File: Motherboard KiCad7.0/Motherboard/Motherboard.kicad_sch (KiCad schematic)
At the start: 59 parts, among them J1 USB_B_Micro, J2 SWD_01x04_Pin, Q7 AO4447A, SW1 SW_STM_RESET, SW2 SW_STM_BOOT_MODE, U1 STM32F103CBT6, U2 AMS1117-3.3, U3 LM66100DCKR, U4 LM66100DCKR, U5 LM66100DCKR, U6 LMR51430XDDCR, Y1 X322516MMB4SI

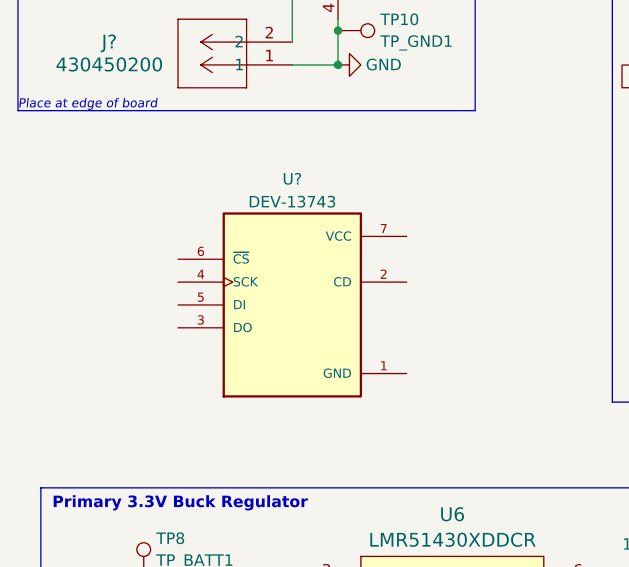
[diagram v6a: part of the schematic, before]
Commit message: Added I2C connector to schematic
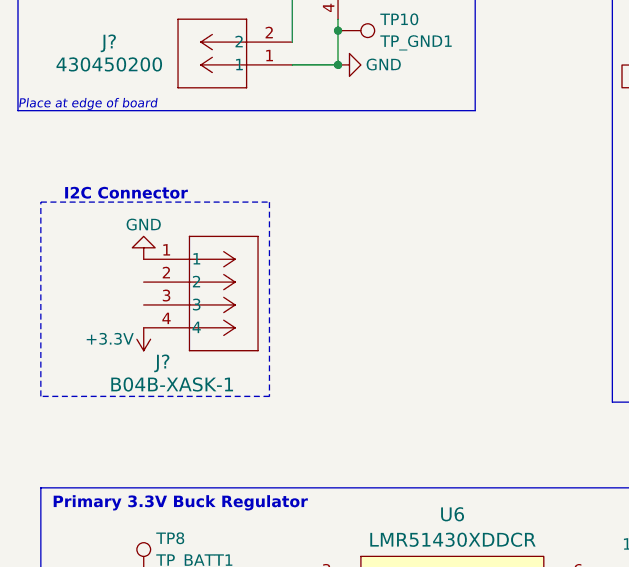
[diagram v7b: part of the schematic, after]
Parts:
- removed U?: DEV-13743, DEV-13743:MODULE_DEV-13743, symbol DEV-13743:DEV-13743
- added J?: B04B-XASK-1, B04B_XASK1:CONN_B04B-XASK-1_JST, symbol B04B_XASK_1:B04B-XASK-1
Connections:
- net +3.3V: now also J?.4
- net GND: now also J?.1
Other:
- note added: "I2C Connector"
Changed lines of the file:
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@@
+    (fill (type none))
+  )
+  (rectangle (start 17.78 52.07) (end 43.18 73.66)
+    (stroke (width 0) (type dash))
     (fill (type none))
   )
@@
   )
   (text "STM32 Decoupling Capacitors for VBAT and VDD" (at 140.97 17.145 0)
+    (effects (font (size 1.27 1.27) (thickness 0.254) bold) (justify left bottom))
+  )
+  (text "I2C Connector" (at 20.32 52.07 0)
     (effects (font (size 1.27 1.27) (thickness 0.254) bold) (justify left bottom))
   )
@@
     )
   )
+  (symbol (lib_id "B04B_XASK_1:B04B-XASK-1") (at 29.21 58.42 0) (unit 1)
+    (in_bom yes) (on_board yes) (dnp no)
+    (property "Reference" "J?" (at 30.48 69.85 0)
+      (effects (font (size 1.524 1.524)) (justify left))
+    )
+    (property "Value" "B04B-XASK-1" (at 25.4 72.39 0)
+      (effects (font (size 1.524 1.524)) (justify left))
+    )
+    (property "Footprint" "B04B_XASK1:CONN_B04B-XASK-1_JST" (at 26.67 52.07 0)
+      (effects (font (size 1.27 1.27) italic) hide)
+    )
+    (property "Datasheet" "B04B-XASK-1" (at 26.67 53.34 0)
+      (effects (font (size 1.27 1.27) italic) hide)
+    )
+    (property "LCSC" "C264994" (at 29.21 58.42 0)
+      (effects (font (size 1.27 1.27)) hide)
+    )
+    (property "Digikey" "455-2150-ND" (at 29.21 58.42 0)
+      (effects (font (size 1.27 1.27)) hide)
+    )
+    (pin "3")
+    (pin "1")
+    (pin "4")
+    (pin "2")
+    (instances
+      (project "Motherboard"
+        (path "/6c6aab7b-9fc7-4161-8073-41667e18c629"
+          (reference "J?") (unit 1)
+        )
+      )
+    )
+  )
   (symbol (lib_id "Switch:SW_Push") (at 54.61 176.53 0) (unit 1)
     (in_bom yes) (on_board yes) (dnp no) (fields_autoplaced)
@@
     )
   )
+  (symbol (lib_id "power:+3.3V") (at 29.21 66.04 0) (mirror x) (unit 1)
+    (in_bom yes) (on_board yes) (dnp no)
+    (property "Reference" "#PWR045" (at 29.21 62.23 0)
+      (effects (font (size 1.27 1.27)) hide)
+    )
+    (property "Value" "+3.3V" (at 25.4 67.31 0)
+      (effects (font (size 1.27 1.27)))
+    )
+    (property "Footprint" "" (at 29.21 66.04 0)
+      (effects (font (size 1.27 1.27)) hide)
+    )
+    (property "Datasheet" "" (at 29.21 66.04 0)
+      (effects (font (size 1.27 1.27)) hide)
+    )
+    (pin "1")
+    (instances
+      (project "Motherboard"
+        (path "/6c6aab7b-9fc7-4161-8073-41667e18c629"
+          (reference "#PWR045") (unit 1)
+        )
+      )
+    )
+  )
   (symbol (lib_id "Connector:TestPoint") (at 109.855 142.24 0) (unit 1)
     (in_bom yes) (on_board yes) (dnp no)
@@
         (path "/6c6aab7b-9fc7-4161-8073-41667e18c629"
           (reference "#PWR04") (unit 1)
+        )
+      )
+    )
+  )
+  (symbol (lib_id "power:GND") (at 29.21 58.42 180) (unit 1)
+    (in_bom yes) (on_board yes) (dnp no)
+    (property "Reference" "#PWR044" (at 29.21 52.07 0)
+      (effects (font (size 1.27 1.27)) hide)
+    )
+    (property "Value" "GND" (at 29.21 54.61 0)
+      (effects (font (size 1.27 1.27)))
+    )
+    (property "Footprint" "" (at 29.21 58.42 0)
+      (effects (font (size 1.27 1.27)) hide)
+    )
+    (property "Datasheet" "" (at 29.21 58.42 0)
+      (effects (font (size 1.27 1.27)) hide)
+    )
+    (pin "1")
+    (instances
+      (project "Motherboard"
+        (path "/6c6aab7b-9fc7-4161-8073-41667e18c629"
+          (reference "#PWR044") (unit 1)
         )
       )
@@
         )
       )
-    )
-  )
-  (symbol (lib_id "DEV-13743:DEV-13743") (at 45.72 63.5 0) (unit 1)
-    (in_bom yes) (on_board yes) (dnp no) (fields_autoplaced)
-    (property "Reference" "U?" (at 45.72 49.53 0)
-      (effects (font (size 1.27 1.27)))
-    )
-    (property "Value" "DEV-13743" (at 45.72 52.07 0)
-      (effects (font (size 1.27 1.27)))
-    )
-    (property "Footprint" "DEV-13743:MODULE_DEV-13743" (at 45.72 63.5 0)
-      (effects (font (size 1.27 1.27)) (justify bottom) hide)
-    )
-    (property "Datasheet" "" (at 45.72 63.5 0)
-      (effects (font (size 1.27 1.27)) hide)
-    )
-    (property "PARTREV" "N/A" (at 45.72 63.5 0)
-      (effects (font (size 1.27 1.27)) (justify bottom) hide)
-    )
-    (property "MANUFACTURER" "Sparkfun Electronics" (at 45.72 63.5 0)
-      (effects (font (size 1.27 1.27)) (justify bottom) hide)
-    )
-    (property "MAXIMUM_PACKAGE_HEIGHT" "6.0 mm" (at 45.72 63.5 0)
-      (effects (font (size 1.27 1.27)) (justify bottom) hide)
-    )
-    (property "STANDARD" "Manufacturer Recommendations" (at 45.72 63.5 0)
-      (effects (font (size 1.27 1.27)) (justify bottom) hide)
-    )
-    (property "Digikey" "1568-1356-ND" (at 45.72 63.5 0)
-      (effects (font (size 1.27 1.27)) hide)
-    )
-    (pin "3")
-    (pin "4")
-    (pin "6")
-    (pin "1")
-    (pin "7")
-    (pin "2")
-    (pin "5")
-    (instances
-      (project "Motherboard"
-        (path "/6c6aab7b-9fc7-4161-8073-41667e18c629"
-          (reference "U?") (unit 1)
-        )
-      )

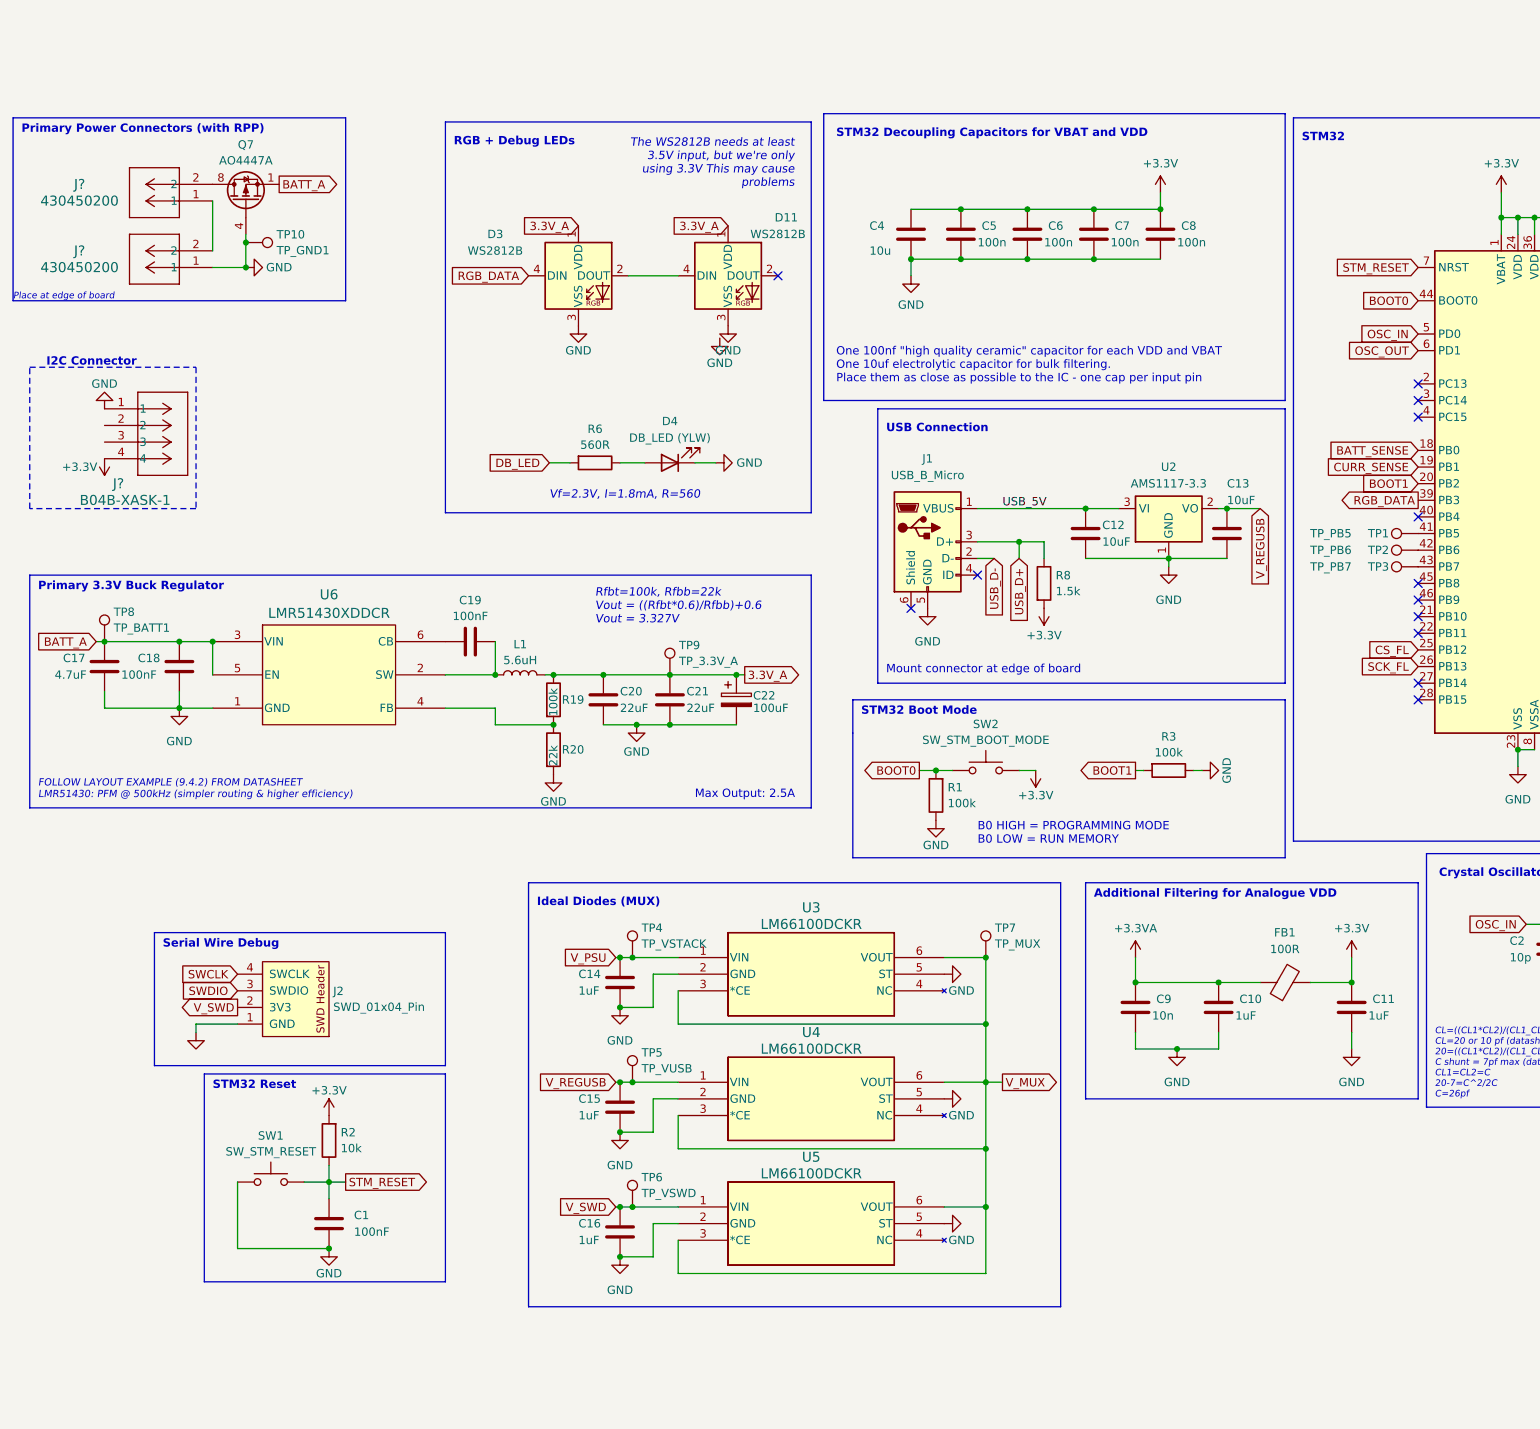
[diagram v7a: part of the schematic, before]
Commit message: Updated symbols and fixed circuit
Updated outdated symbols and replaced 3.3V buck converter circuit with a module.
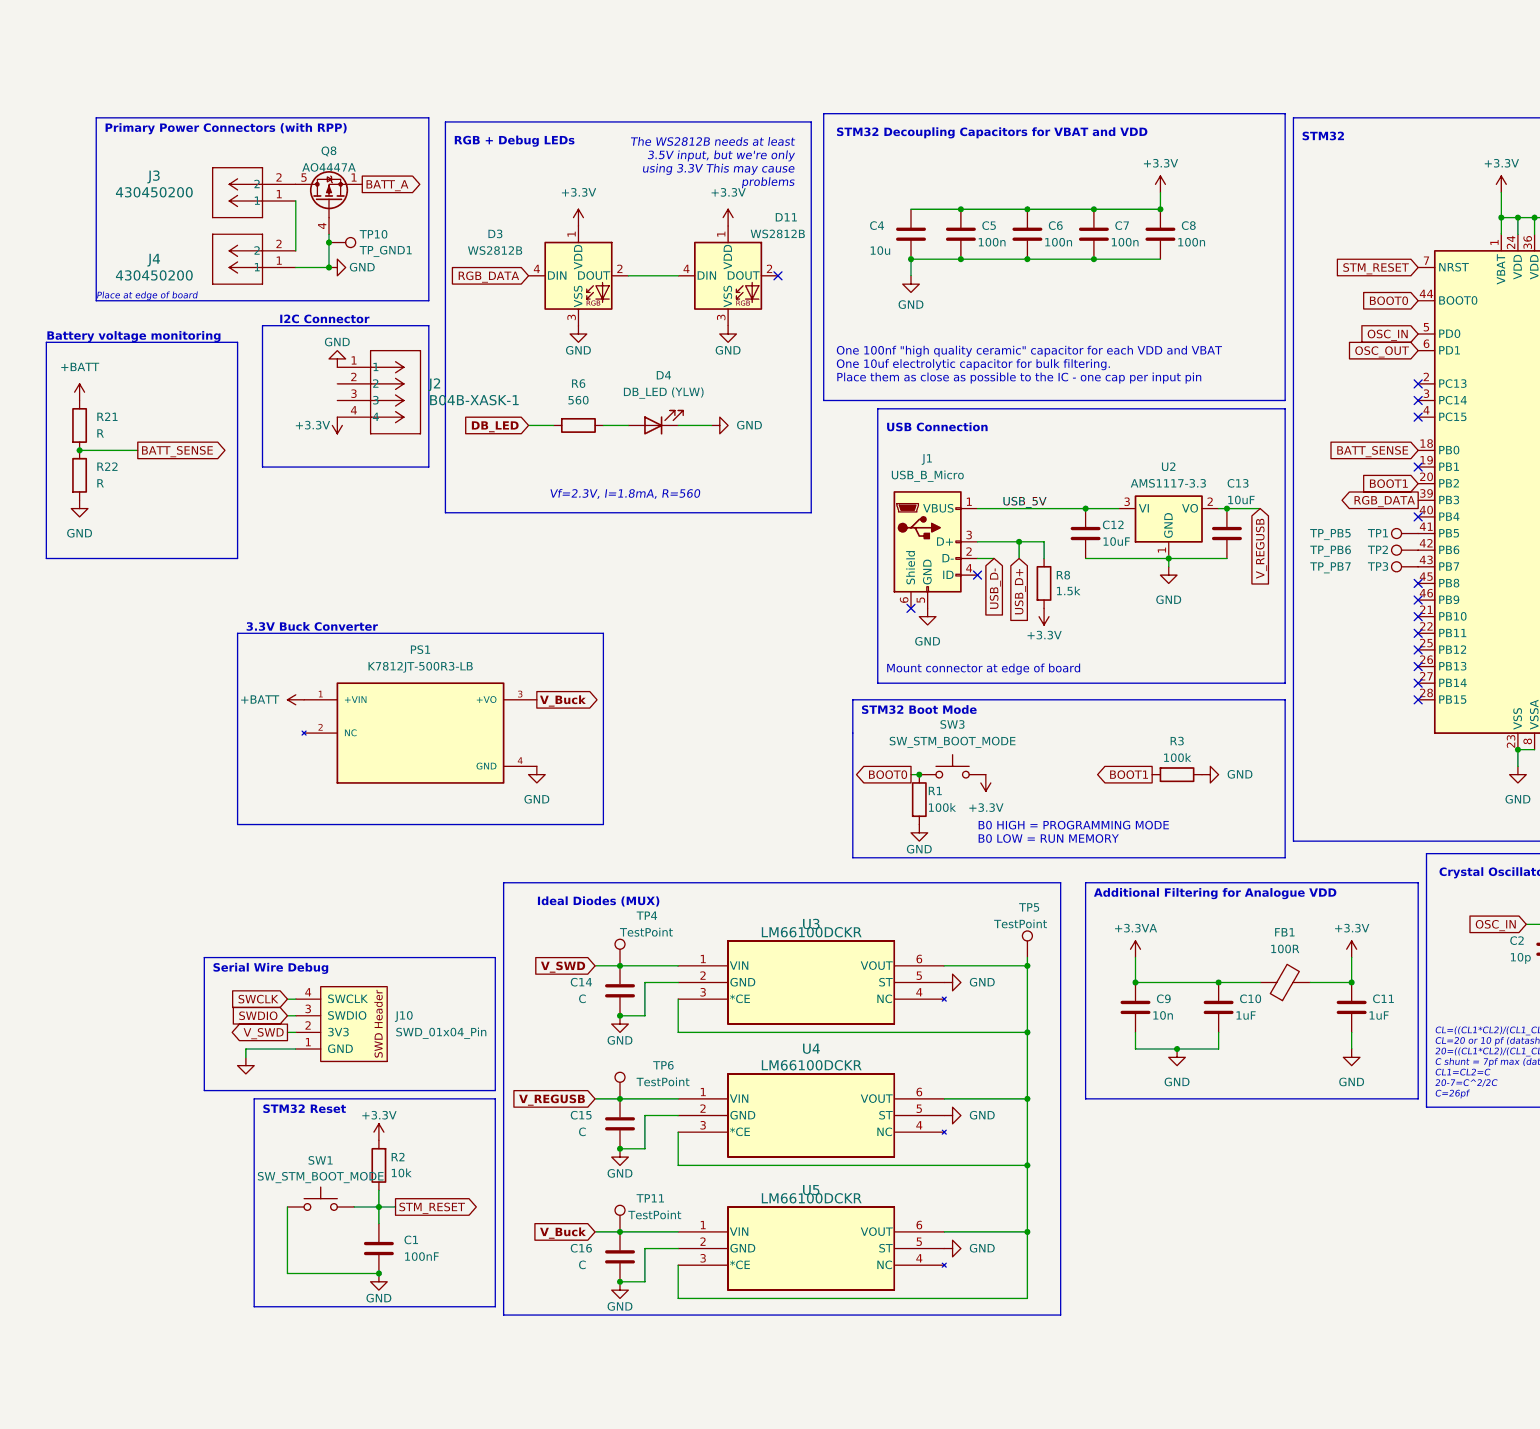
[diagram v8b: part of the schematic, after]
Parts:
- removed C17: 4.7uF, Capacitor_SMD:C_0805_2012Metric, symbol Device:C
- removed C18, C19: 100nF, Capacitor_SMD:C_0603_1608Metric, symbol Device:C
- removed C20, C21: 22uF, Capacitor_SMD:C_0805_2012Metric, symbol Device:C
- removed C22: 100uF, Capacitor_SMD:CP_Elec_6.3x5.9, symbol Device:C_Polarized
- removed J2: SWD_01x04_Pin, SWD_Header:SWD_PinHeader_1x04_P2.54mm_Horizontal, symbol QRET_Edge_Connector:SWD_01x04_Pin
- removed J?: B04B-XASK-1, B04B_XASK1:CONN_B04B-XASK-1_JST, symbol B04B_XASK_1:B04B-XASK-1
- removed J? (x2): 430450200, CONN 0430450200:CON_430450200_MOL, symbol CONN 0430450200:430450200
- removed L1: 5.6uH, Inductor_SMD:L_Bourns_SRN8040TA, symbol Device:L
- removed Q7: AO4447A, Package_SO:SOIC-8_3.9x4.9mm_P1.27mm, symbol Transistor_FET:IRF7404
- removed R19: 100k, Resistor_SMD:R_0603_1608Metric, symbol Device:R
- removed R20: 22k, Resistor_SMD:R_0603_1608Metric, symbol Device:R
- removed SW2: SW_STM_BOOT_MODE, PTS636:PTS636_SK43_SMTR_LFS, symbol Switch:SW_Push
- removed TP7: TP_MUX, TestPoint:TestPoint_Pad_1.5x1.5mm, symbol Connector:TestPoint
- removed TP8: TP_BATT1, TestPoint:TestPoint_Pad_2.0x2.0mm, symbol Connector:TestPoint
- removed TP9: TP_3.3V_A, TestPoint:TestPoint_Pad_2.0x2.0mm, symbol Connector:TestPoint
- removed U3, U4, U5: LM66100DCKR, LMR66100:SC-70-6, symbol QRET_Buck_PSU:LM66100DCKR
- removed U6: LMR51430XDDCR, Package_TO_SOT_SMD:SOT-23-6_Handsoldering, symbol QRET_Buck_PSU-symbols:LMR51430XDDCR
- added J10: SWD_01x04_Pin, SWD_Header:SWD_PinHeader_1x04_P2.54mm_Horizontal, symbol EdgeConnector:SWD_01x04_Pin
- added J2: B04B-XASK-1, CONN_B04B-XASK-1_JST, symbol B04B_XASK_1:B04B-XASK-1
- added J3, J4: 430450200, CON_430450200_MOL, symbol CONN 0430450200:430450200
- added PS1: K7812JT-500R3-LB, K7812JT-500R3-LB:CONV_K7812JT-500R3-LB, symbol K7812JT-500R3-LB:K7812JT-500R3-LB
- added Q8: AO4447A, Package_SO:SOIC-8_3.9x4.9mm_P1.27mm, symbol Transistor_FET:IRF7404
- added R21, R22: R, symbol Device:R
- added SW3: SW_STM_BOOT_MODE, Button_Switch_SMD:SW_Push_1P1T_XKB_TS-1187A, symbol Switch:SW_MEC_5G
- added TP11: TestPoint, symbol Connector:TestPoint
- added U3, U4, U5: LM66100DCKR, LMR66100:SC-70-6_Handsoldering, symbol QRET_Buck_PSU-symbols:LM66100DCKR
- C14, C15, C16: value 1uF -> C; footprint Capacitor_SMD:C_0603_1608Metric -> (none); LCSC C15849 -> (none)
- D4: footprint LED_SMD:LED_0603_1608Metric -> (none); LCSC C72038 -> (none)
- R1, R3: footprint Resistor_SMD:R_0603_1608Metric -> (none); LCSC C25803 -> (none)
- R6: value 560R -> 560; footprint Resistor_SMD:R_0603_1608Metric -> (none); LCSC C23204 -> (none)
- SW1: value SW_STM_RESET -> SW_STM_BOOT_MODE; footprint PTS636:PTS636_SK43_SMTR_LFS -> Button_Switch_SMD:SW_Push_1P1T_XKB_TS-1187A
- TP4: value TP_VSTACK -> TestPoint; footprint TestPoint:TestPoint_Pad_1.5x1.5mm -> (none)
- TP5: value TP_VUSB -> TestPoint; footprint TestPoint:TestPoint_Pad_1.5x1.5mm -> (none)
- TP6: value TP_VSWD -> TestPoint; footprint TestPoint:TestPoint_Pad_1.5x1.5mm -> (none)
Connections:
- net 3.3V_A is gone; now on net +3.3V: D11.1 (VDD), D3.1 (VDD)
- net V_PSU is gone; now on net V_SWD: C14.1, TP4.1
- net +3.3V: now also J2.4, SW3.3 (B), SW3.4 (B)
- net BATT_A: now also Q8.1 (S), Q8.2 (S), Q8.3 (S)
- net BATT_SENSE: now also R21.2, R22.1
- net BOOT0: now also R1.1, SW3.1 (A), SW3.2 (A); no longer R1.2
- net GND: now also R1.2, J10.1 (GND), J2.1, J4.1, PS1.4 (GND), Q8.4 (G), R22.2, U3.2 (GND), U3.5 (ST), U4.2 (GND), U4.5 (ST), U5.2 (GND), U5.5 (ST); no longer R1.1
- net SWCLK: now also J10.4 (SWCLK)
- net SWDIO: now also J10.3 (SWDIO)
- net V_REGUSB: now also TP6.1, U4.1 (VIN); no longer TP5.1
- net V_SWD: now also J10.2 (3V3), U3.1 (VIN); no longer C16.1, TP6.1
- net CS_FL: no longer names the net of U1.25 (PB12)
- net CURR_SENSE: no longer names the net of U1.19 (PB1)
- net SCK_FL: no longer names the net of U1.26 (PB13)
- new net: TP5.1, U3.3 (*CE), U3.6 (VOUT), U4.3 (*CE), U4.6 (VOUT), U5.3 (*CE), U5.6 (VOUT)
- new net: J3.1, J4.2
- new net: J3.2, Q8.5 (D), Q8.6 (D), Q8.7 (D), Q8.8 (D)
- new net +BATT: PS1.1 (+VIN), R21.1
- new net V_Buck: C16.1, PS1.3 (+VO), TP11.1, U5.1 (VIN)
- no-connect marks 18 -> 21
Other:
- note added: "3.3V Buck Converter"
- note added: "Battery voltage monitoring"
- note removed: "FOLLOW LAYOUT EXAMPLE (9.4.2) FROM DATASHEET LMR51430: PFM @ 500kHz (simpler routing & higher efficiency)"
- note removed: "Max Output: 2.5A"
- note removed: "Primary 3.3V Buck Regulator"
- note removed: "Rfbt=100k, Rfbb=22k Vout = ((Rfbt*0.6)/Rfbb)+0.6 Vout = 3.327V"
- moved on the sheet: C1, R2, TP10
